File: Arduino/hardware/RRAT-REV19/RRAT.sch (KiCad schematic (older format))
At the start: 38 parts, among them IC1 ATMEGA168-AU, J1 Conn_01x06, J2 Conn_02x03_Odd_Even, J3 Conn_02x20_Odd_Even, J4 Conn_01x12, Q1 32768Hz, U1 RFM26, U2 MIC94092YC6

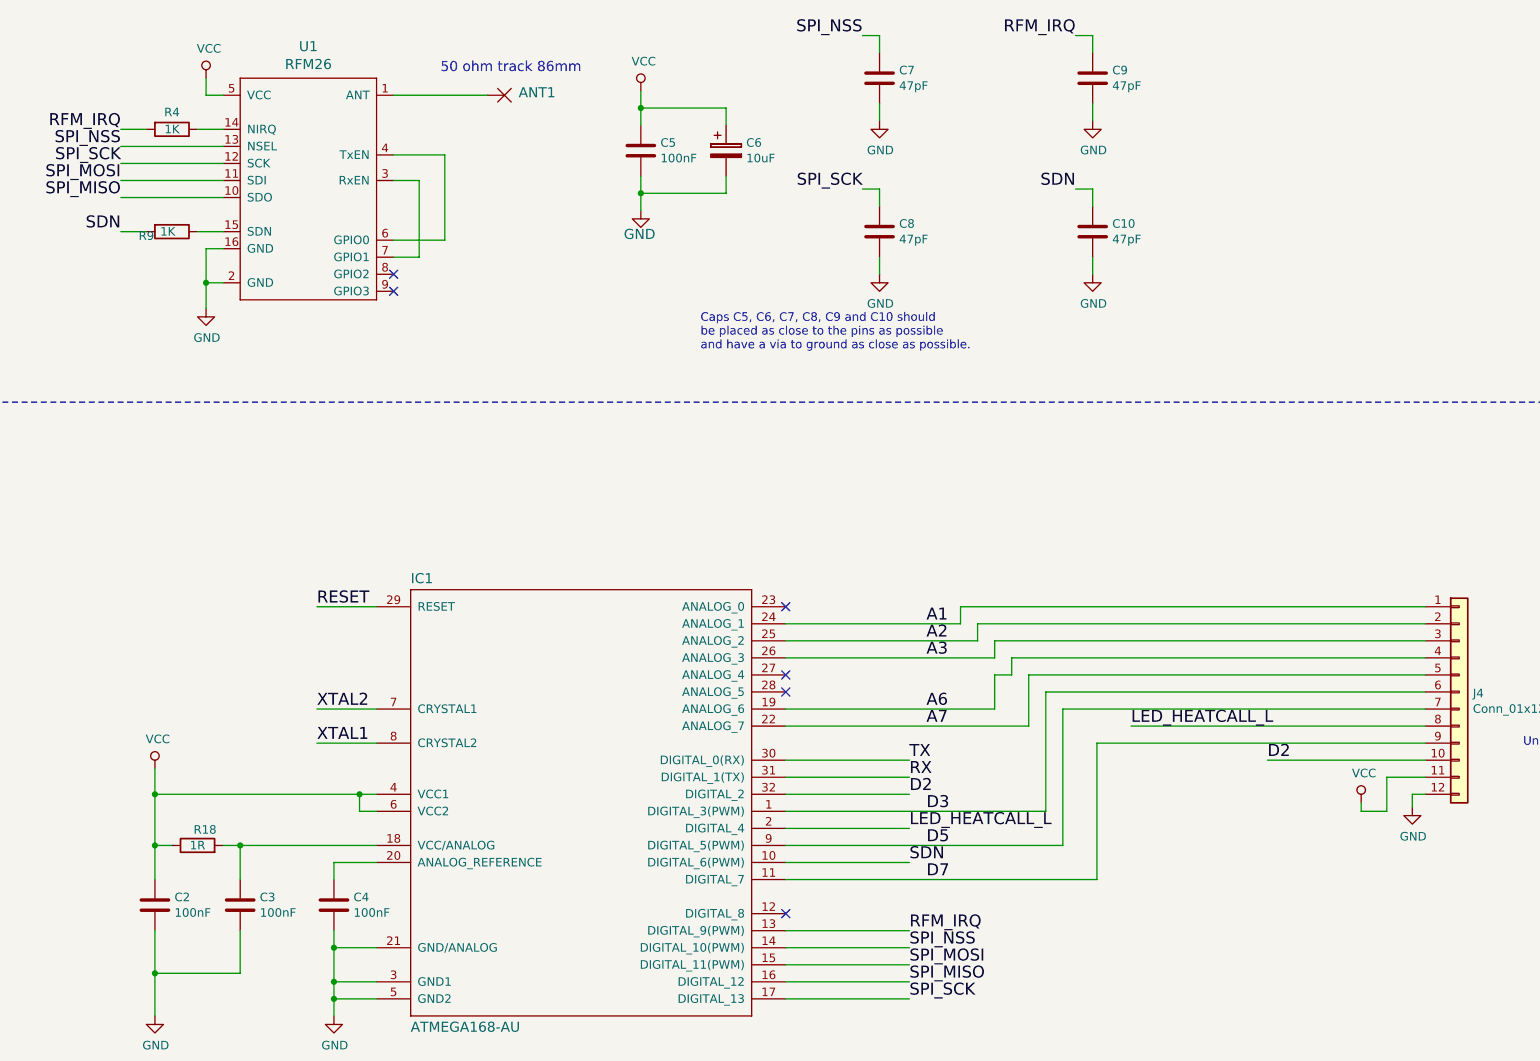
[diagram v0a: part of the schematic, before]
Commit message: Decoupling fixes + some routing
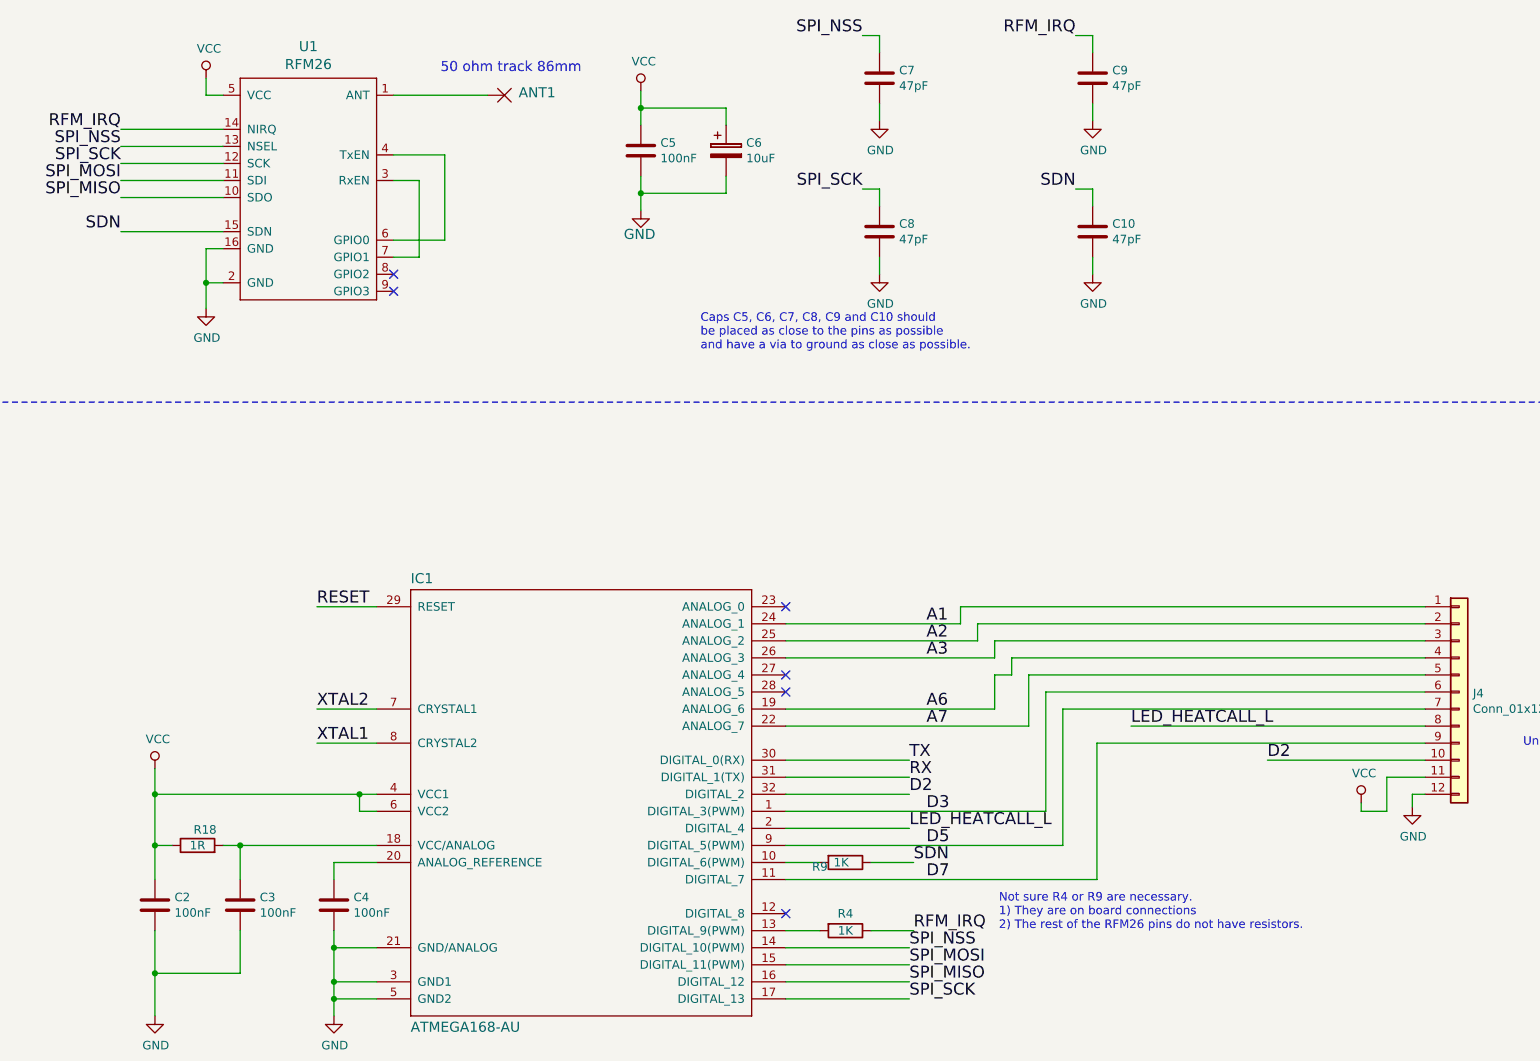
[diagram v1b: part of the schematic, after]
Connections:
- net RFM_IRQ: now also R4.1, U1.14 (NIRQ); no longer IC1.13 (DIGITAL_9(PWM)), R4.2
- net SDN: now also R9.1, U1.15 (SDN); no longer IC1.10 (DIGITAL_6(PWM)), R9.2
- new net: IC1.13 (DIGITAL_9(PWM)), R4.2
- new net: IC1.10 (DIGITAL_6(PWM)), R9.2
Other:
- note added: "Not sure R4 or R9 are necessary.\n1) They are on board connections\n2) The rest of the RFM26 pins do not have resistors."
- moved on the sheet: R4, R9
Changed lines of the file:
@@
 EESchema Schematic File Version 4
 LIBS:RRAT-cache
-EELAYER 29 0
+EELAYER 26 0
 EELAYER END
 $Descr User 17018 11968
@@
 Comment4 ""
 $EndDescr
-Wire Wire Line
-	10900 5600 11625 5600
 Wire Wire Line
 	10900 6400 11625 6400
@@
 Text Label 11625 5100 0    70   ~ 0
 RX
-Wire Wire Line
-	10900 6000 11625 6000
-Text Label 11625 6000 0    70   ~ 0
+Text Label 11650 6000 0    70   ~ 0
 RFM_IRQ
 Text Label 12600 750  2    70   ~ 0
@@
 L RRAT_consolidated:R R4
 U 1 1 5BBBC122
-P 7300 1300
-F 0 "R4" V 7200 1300 50  0000 C CNN
-F 1 "1K" V 7300 1300 50  0000 C CNN
-F 2 "RRAT Consolidated:R0603" V 7230 1300 50  0001 C CNN
-F 3 "~" H 7300 1300 50  0001 C CNN
-	1    7300 1300
+P 11250 6000
+F 0 "R4" V 11150 6000 50  0000 C CNN
+F 1 "1K" V 11250 6000 50  0000 C CNN
+F 2 "RRAT Consolidated:R0603" V 11180 6000 50  0001 C CNN
+F 3 "~" H 11250 6000 50  0001 C CNN
+	1    11250 6000
 	0    1    1    0
 $EndComp
@@
 	1    0    0    -1
 $EndComp
-Text Label 11625 5600 0    70   ~ 0
+Text Label 11650 5600 0    70   ~ 0
 SDN
 $Comp
 L RRAT_consolidated:R R9
 U 1 1 5BBE9C11
-P 7300 1900
-F 0 "R9" V 7325 1750 50  0000 C CNN
-F 1 "1K" V 7300 1875 50  0000 C CNN
-F 2 "RRAT Consolidated:R0603" V 7230 1900 50  0001 C CNN
-F 3 "~" H 7300 1900 50  0001 C CNN
-	1    7300 1900
+P 11250 5600
+F 0 "R9" V 11275 5450 50  0000 C CNN
+F 1 "1K" V 11250 5575 50  0000 C CNN
+F 2 "RRAT Consolidated:R0603" V 11180 5600 50  0001 C CNN
+F 3 "~" H 11250 5600 50  0001 C CNN
+	1    11250 5600
 	0    1    1    0
 $EndComp
@@
 	7500 1100 7600 1100
 Wire Wire Line
-	7000 1300 7150 1300
-Wire Wire Line
-	7450 1300 7600 1300
-Wire Wire Line
 	7000 1400 7600 1400
 Wire Wire Line
@@
 $EndComp
 Wire Wire Line
-	7000 1900 7150 1900
-Wire Wire Line
-	7450 1900 7600 1900
-Wire Wire Line
 	7600 2000 7500 2000
 Wire Wire Line
@@
 Text Notes 4650 2800 0    50   ~ 0
 NOTE:\nSpecial considerations on placement\nand keepouts.\n\nSee existing designs.
+Wire Wire Line
+	7000 1300 7600 1300
+Wire Wire Line
+	11650 6000 11400 6000
+Wire Wire Line
+	11100 6000 10900 6000
+Text Notes 12150 6000 0    50   ~ 0
+Not sure R4 or R9 are necessary.\n1) They are on board connections\n2) The rest of the RFM26 pins do not have resistors.
+Wire Wire Line
+	10900 5600 11100 5600
+Wire Wire Line
+	11400 5600 11650 5600
+Wire Wire Line
+	7600 1900 7000 1900
 $EndSCHEMATC

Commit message: RRAT-PCB-REV-A
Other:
- note added: "Copyright: Bo Herrmannsen 2018, Deniz Erbilgin + Damon Hart-Davis 2019"
- note removed: "Copyright: Bo Herrmannsen 2018, Deniz Erbilgin 2019"
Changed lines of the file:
@@
 EESchema Schematic File Version 4
 LIBS:RRAT-cache
-EELAYER 26 0
+EELAYER 29 0
 EELAYER END
 $Descr User 17018 11968
 encoding utf-8
 Sheet 1 1
-Title ""
-Date ""
-Rev ""
-Comp ""
+Title "RRAT"
+Date "2019-05-30"
+Rev "A"
+Comp "OpenTRV"
 Comment1 ""
 Comment2 ""
@@
 	2700 700  2700 2900
 Text Notes 1200 11000 0    59   ~ 0
-Copyright: Bo Herrmannsen 2018, Deniz Erbilgin 2019
+Copyright: Bo Herrmannsen 2018, Deniz Erbilgin + Damon Hart-Davis 2019
 $Comp
 L RRAT_consolidated:Conn_02x03_Odd_Even J2

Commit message: updates and fixes
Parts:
- removed C6: 10uF, RRAT Consolidated:EIA3216, symbol RRAT_consolidated:CP
- added C6: 100uF, Capacitor_SMD:C_1206_3216Metric, symbol RRAT_consolidated:C
- ANT1, JP1: Part-No (none) -> N/A; Tolerance (none) -> N/A
- C1, C14, C2, C3, C4, C5: Part-No (none) -> C0603C104K4RAC; Tolerance (none) -> 10%
- C10, C7, C8, C9: Part-No (none) -> 0603N470J500NT; Tolerance (none) -> 5%
- C11, C12, C13: Part-No (none) -> DNF; Tolerance (none) -> N/A
- IC1: value ATMEGA168-AU -> ATmega328P-AU; Part-No (none) -> ATmega328P-AU; Tolerance (none) -> N/A
- J1, J2, J3: Tolerance (none) -> N/A
- J4: Part-No (none) -> W81136T3816RC; Tolerance (none) -> N/A
- Q1: Part-No (none) -> QTC332.76812B2R; Tolerance (none) -> 20ppm
- R1, R2, R5: Part-No (none) -> CRG0603F4K7; Tolerance (none) -> 1%
- R10, R12, R13, R14, R15, R16, R17, R3, R4, R9: Part-No (none) -> CRG0603F1K0; Tolerance (none) -> 1%
- R18: Part-No (none) -> RC0603FR-071RL; Tolerance (none) -> 1%
- U1: value RFM26 -> RFM26W-868S2; Part-No (none) -> RFM26W-868S2; Tolerance (none) -> N/A
- U2: Part-No (none) -> MIC94092YC6; Tolerance (none) -> N/A
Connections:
- net GND: now also R3.1, C6.2; no longer R3.2
- net VCC: now also C6.1
- net at J1.2 (Pin_2): now also R3.2; no longer R3.1
